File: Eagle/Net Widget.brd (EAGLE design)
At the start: 76.2 x 45.7 mm, 19 parts, among them IC1 ATmega1284P

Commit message: Tweak.
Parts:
- moved R1 26.5 mm to (71.8, 34.3)
- moved R2 6.55 mm to (47.3, 32.7)
- moved R3 6.55 mm to (47.3, 30.2)
- moved R5 6.55 mm to (47.3, 27.6)
- moved R6 0.64 mm to (67.6, 24.1)
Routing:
- net TOUCH: track 10.0 -> 9.40 mm
- net N$1: track 4.18 -> 3.55 mm
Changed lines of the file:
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@@
 <vertex x="62.23" y="35.56"/>
 </polygon>
-<rectangle x1="69.85" y1="17.78" x2="76.2" y2="29.21" layer="41"/>
 <polygon width="0.4064" layer="42">
 <vertex x="76.2" y="29.21"/>
-<vertex x="69.85" y="29.21"/>
-<vertex x="69.85" y="25.0825"/>
+<vertex x="68.58" y="29.21"/>
+<vertex x="68.58" y="25.0825"/>
 <vertex x="62.23" y="25.0825"/>
 <vertex x="62.23" y="23.495"/>
 <vertex x="64.4525" y="23.495"/>
 <vertex x="64.4525" y="21.9075"/>
-<vertex x="69.85" y="21.9075"/>
-<vertex x="69.85" y="17.78"/>
+<vertex x="68.58" y="21.9075"/>
+<vertex x="68.58" y="17.78"/>
 <vertex x="76.2" y="17.78"/>
+</polygon>
+<polygon width="0.4064" layer="41">
+<vertex x="76.2" y="17.78"/>
+<vertex x="68.58" y="17.78"/>
+<vertex x="68.58" y="29.21"/>
+<vertex x="76.2" y="29.21"/>
 </polygon>
 </plain>
@@
 <element name="LED1" library="SparkFun-LED" package="LED-TRICOLOR-5050" value="LED-TRICOLOR-5050NO_IC" x="38.1" y="22.86" rot="R180"/>
 <element name="LED2" library="led" package="1206" value="" x="71.755" y="31.4325"/>
-<element name="R1" library="rcl" package="R1206" value="100" x="45.72" y="29.21"/>
-<element name="R2" library="rcl" package="R1206" value="100" x="45.72" y="26.3525"/>
-<element name="R3" library="rcl" package="R1206" value="100" x="45.72" y="23.8125"/>
-<element name="R5" library="rcl" package="R1206" value="100" x="45.72" y="21.2725"/>
-<element name="R6" library="rcl" package="R1206" value="1M" x="68.2625" y="24.13" rot="R180"/>
+<element name="R1" library="rcl" package="R1206" value="100" x="71.755" y="34.29"/>
+<element name="R2" library="rcl" package="R1206" value="100" x="47.3075" y="32.7025"/>
+<element name="R3" library="rcl" package="R1206" value="100" x="47.3075" y="30.1625"/>
+<element name="R5" library="rcl" package="R1206" value="100" x="47.3075" y="27.6225"/>
+<element name="R6" library="rcl" package="R1206" value="1M" x="67.6275" y="24.13" rot="R180"/>
 </elements>
 <signals>
@@
 <contactref element="IC1" pad="13"/>
 <contactref element="R1" pad="2"/>
-<wire x1="47.142" y1="29.21" x2="51.6675" y2="31.14" width="0" layer="19" extent="1-1"/>
+<wire x1="73.177" y1="34.29" x2="51.6675" y2="31.14" width="0" layer="19" extent="1-1"/>
 </signal>
 <signal name="B">
 <contactref element="IC1" pad="14"/>
 <contactref element="R2" pad="2"/>
-<wire x1="47.142" y1="26.3525" x2="51.6675" y2="30.34" width="0" layer="19" extent="1-1"/>
+<wire x1="48.7295" y1="32.7025" x2="51.6675" y2="30.34" width="0" layer="19" extent="1-1"/>
 </signal>
 <signal name="R">
 <contactref element="IC1" pad="15"/>
 <contactref element="R3" pad="2"/>
-<wire x1="47.142" y1="23.8125" x2="51.6675" y2="29.54" width="0" layer="19" extent="1-1"/>
+<wire x1="48.7295" y1="30.1625" x2="51.6675" y2="29.54" width="0" layer="19" extent="1-1"/>
 </signal>
 <signal name="G">
 <contactref element="IC1" pad="16"/>
 <contactref element="R5" pad="2"/>
-<wire x1="47.142" y1="21.2725" x2="51.6675" y2="28.74" width="0" layer="19" extent="1-1"/>
+<wire x1="48.7295" y1="27.6225" x2="51.6675" y2="28.74" width="0" layer="19" extent="1-1"/>
 </signal>
 <signal name="N$9">
 <contactref element="R1" pad="1"/>
 <contactref element="LED2" pad="A"/>
-<wire x1="44.298" y1="29.21" x2="70.333" y2="31.4325" width="0" layer="19" extent="1-1"/>
+<wire x1="70.333" y1="34.29" x2="70.333" y2="31.4325" width="0" layer="19" extent="1-1"/>
 </signal>
 <signal name="TOUCH">
@@
 <polygon width="0.4064" layer="1">
 <vertex x="76.2" y="29.21"/>
-<vertex x="69.85" y="29.21"/>
-<vertex x="69.85" y="17.78"/>
+<vertex x="68.8975" y="29.21"/>
+<vertex x="68.8975" y="17.78"/>
 <vertex x="76.2" y="17.78"/>
 </polygon>
@@
 <wire x1="63.2675" y1="23.94" x2="64.77" y2="23.94" width="0.3048" layer="1"/>
 <wire x1="64.77" y1="23.94" x2="64.77" y2="22.225" width="0.3048" layer="1"/>
-<wire x1="64.77" y1="22.225" x2="69.6845" y2="22.225" width="0.3048" layer="1"/>
-<wire x1="69.6845" y1="22.225" x2="69.6845" y2="24.13" width="0.3048" layer="1"/>
+<wire x1="64.77" y1="22.225" x2="69.0495" y2="22.225" width="0.3048" layer="1"/>
+<wire x1="69.0495" y1="22.225" x2="69.0495" y2="24.13" width="0.3048" layer="1"/>
 </signal>
 <signal name="N$1">
 <contactref element="IC1" pad="35"/>
 <contactref element="R6" pad="2"/>
-<wire x1="63.2675" y1="24.74" x2="66.8405" y2="24.74" width="0.3048" layer="1"/>
-<wire x1="66.8405" y1="24.74" x2="66.8405" y2="24.13" width="0.3048" layer="1"/>
+<wire x1="63.2675" y1="24.74" x2="66.2055" y2="24.74" width="0.3048" layer="1"/>
+<wire x1="66.2055" y1="24.74" x2="66.2055" y2="24.13" width="0.3048" layer="1"/>
 </signal>
 <signal name="N$2">
 <contactref element="R3" pad="1"/>
 <contactref element="LED1" pad="2"/>
-<wire x1="40.5" y1="22.86" x2="44.298" y2="23.8125" width="0" layer="19" extent="1-1"/>
+<wire x1="40.5" y1="22.86" x2="45.8855" y2="30.1625" width="0" layer="19" extent="1-1"/>
 </signal>
 <signal name="N$4">
 <contactref element="R5" pad="1"/>
 <contactref element="LED1" pad="1"/>
-<wire x1="40.5" y1="21.16" x2="44.298" y2="21.2725" width="0" layer="19" extent="1-1"/>
+<wire x1="40.5" y1="21.16" x2="45.8855" y2="27.6225" width="0" layer="19" extent="1-1"/>
 </signal>
 <signal name="N$5">
 <contactref element="R2" pad="1"/>
 <contactref element="LED1" pad="3"/>
-<wire x1="40.5" y1="24.56" x2="44.298" y2="26.3525" width="0" layer="19" extent="1-1"/>
+<wire x1="40.5" y1="24.56" x2="45.8855" y2="32.7025" width="0" layer="19" extent="1-1"/>
 </signal>
 </signals>

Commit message: ...
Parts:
- moved R1 24.5 mm to (47.3, 33.0)
- moved R4 6.74 mm to (60.0, 34.0), turned to 180 degrees
- moved C1 5.39 mm to (48.3, 13.0)
- moved IC1 2.54 mm to (57.5, 25.4)
- moved R3 2.54 mm to (47.3, 27.6)
- moved C5 2.54 mm to (58.1, 16.5)
- moved R2 2.54 mm to (47.3, 30.2)
- moved R5 2.54 mm to (47.3, 25.1)
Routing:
- net N$6: track 0.00 -> 7.03 mm
- net N$7: track 0.00 -> 6.83 mm
- net N$1: track 3.55 -> 5.53 mm
- net TOUCH: track 9.40 -> 8.51 mm

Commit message: Route.
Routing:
- net GND: track 10.2 -> 182.3 mm, vias 0 -> 1
- net VCC: track 0.00 -> 123.7 mm, vias 0 -> 4
- net CS: track 0.00 -> 92.8 mm
- net IRQ: track 0.00 -> 84.3 mm, vias 0 -> 2
- net MOSI: track 0.00 -> 78.5 mm, vias 0 -> 1
- net VBEN: track 0.00 -> 74.4 mm, vias 0 -> 2
- net RESET: track 0.00 -> 69.5 mm
- net SCK: track 0.00 -> 62.5 mm
- net MISO: track 0.00 -> 57.7 mm, vias 0 -> 1
- net TX: track 0.00 -> 34.3 mm, vias 0 -> 1
- net N$9: track 0.00 -> 28.6 mm, vias 0 -> 2
- net RX: track 0.00 -> 22.5 mm
- net N$5: track 0.00 -> 7.86 mm
- net N$2: track 0.00 -> 7.37 mm
- net N$4: track 0.00 -> 7.02 mm
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
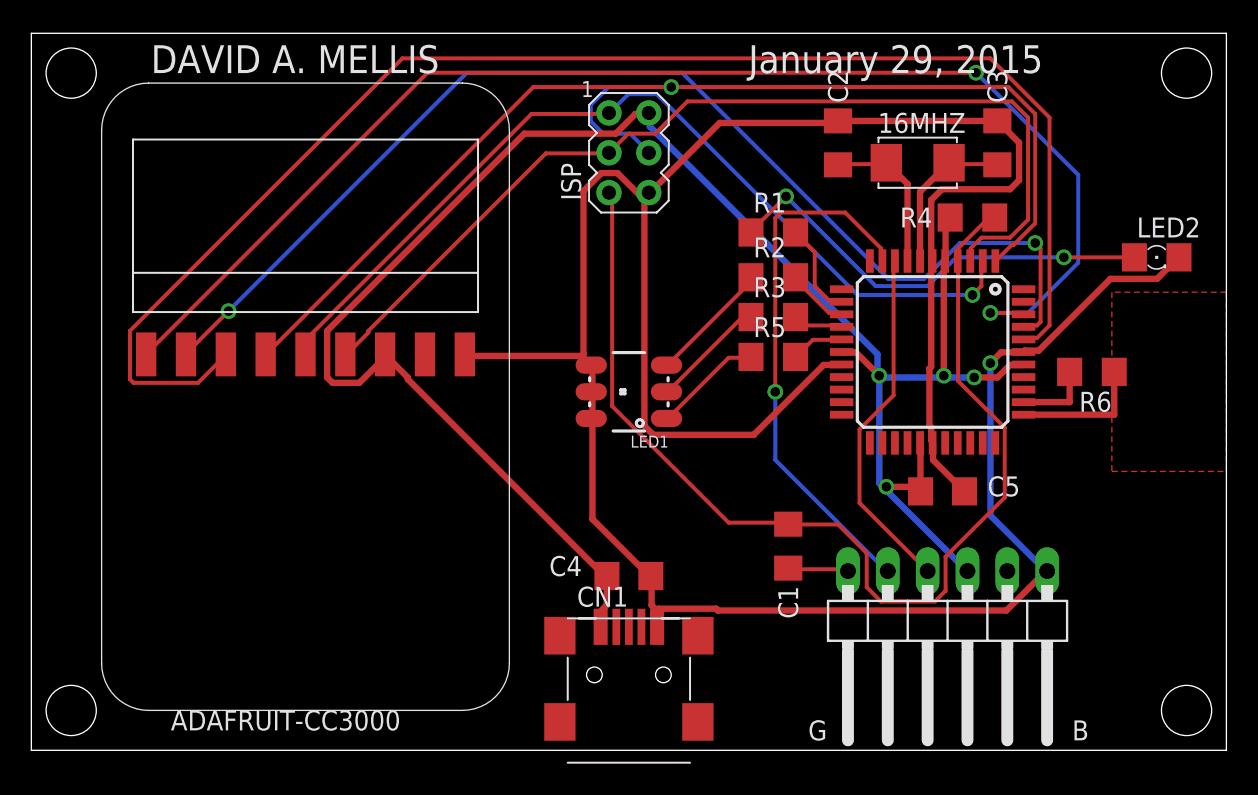
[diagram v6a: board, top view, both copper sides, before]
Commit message: Add alligator clip connector and adjust silkscreen
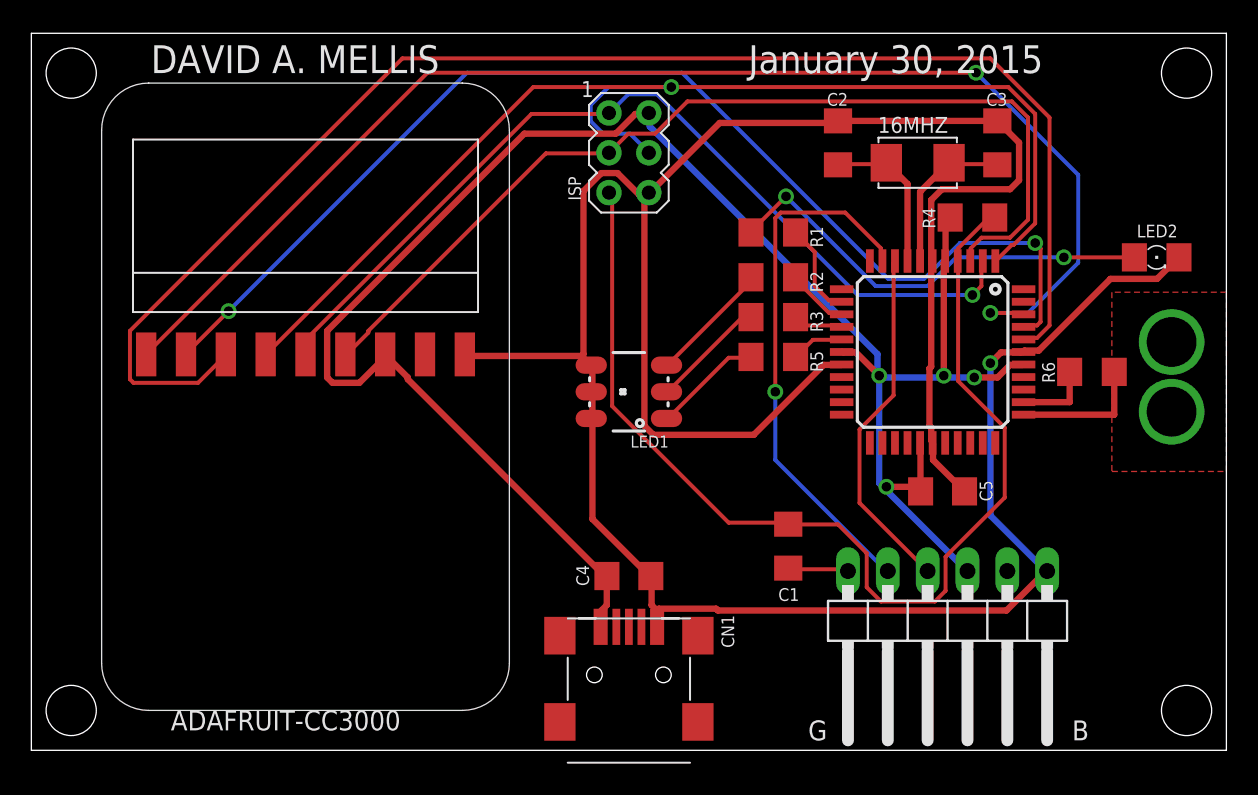
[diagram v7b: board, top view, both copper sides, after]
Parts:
- added TOUCH: (no value), SparkFun-Connectors:1X01_ALLIGATOR_3MM
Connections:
- net TOUCH: now also TOUCH.1@0, TOUCH.1@2
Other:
- board text added: "January 30, 2015"
- board text removed: "January 29, 2015"
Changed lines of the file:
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@@
 <layer number="27" name="tValues" color="7" fill="1" visible="yes" active="yes"/>
 <layer number="28" name="bValues" color="7" fill="1" visible="yes" active="yes"/>
-<layer number="29" name="tStop" color="7" fill="3" visible="no" active="yes"/>
-<layer number="30" name="bStop" color="7" fill="6" visible="no" active="yes"/>
+<layer number="29" name="tStop" color="7" fill="3" visible="yes" active="yes"/>
+<layer number="30" name="bStop" color="7" fill="6" visible="yes" active="yes"/>
 <layer number="31" name="tCream" color="7" fill="4" visible="no" active="yes"/>
 <layer number="32" name="bCream" color="7" fill="5" visible="no" active="yes"/>
@@
 <text x="8.89" y="1.27" size="1.27" layer="25" font="fixed">ADAFRUIT-CC3000</text>
 <text x="7.62" y="43.18" size="1.778" layer="25" font="fixed">DAVID A. MELLIS</text>
-<text x="45.72" y="43.18" size="1.778" layer="25" font="fixed">January 29, 2015</text>
+<text x="45.72" y="43.18" size="1.778" layer="25" font="fixed">January 30, 2015</text>
 <text x="66.3575" y="0.635" size="1.27" layer="25" font="fixed" rot="SR0">B</text>
 <text x="49.53" y="0.635" size="1.27" layer="25" font="fixed" rot="SR0">G</text>
@@
 <elements>
 <element name="C2" library="rcl" package="C1206" value="18pF" x="51.435" y="38.735" smashed="yes" rot="R270">
-<attribute name="NAME" x="52.07" y="41.275" size="1.27" layer="25" font="fixed" rot="R90"/>
-<attribute name="VALUE" x="49.2125" y="40.9575" size="1.27" layer="27" font="fixed" rot="R270"/>
+<attribute name="NAME" x="52.07" y="41.91" size="0.8128" layer="25" font="fixed" rot="R180"/>
+<attribute name="VALUE" x="49.2125" y="40.9575" size="1.016" layer="27" font="fixed" rot="R270"/>
 </element>
 <element name="C3" library="rcl" package="C1206" value="18pF" x="61.595" y="38.735" smashed="yes" rot="R270">
-<attribute name="NAME" x="62.23" y="41.275" size="1.27" layer="25" font="fixed" rot="R90"/>
-<attribute name="VALUE" x="62.5475" y="40.9575" size="1.27" layer="27" font="fixed" rot="R270"/>
+<attribute name="NAME" x="62.23" y="41.91" size="0.8128" layer="25" font="fixed" rot="R180"/>
+<attribute name="VALUE" x="62.5475" y="40.3225" size="1.016" layer="27" font="fixed" rot="R270"/>
 </element>
 <element name="ISP" library="adafruit" package="AVRISP" value="AVRISP-6" x="38.1" y="38.1" smashed="yes">
-<attribute name="NAME" x="35.052" y="35.052" size="1.27" layer="25" font="fixed" rot="R90"/>
+<attribute name="NAME" x="35.052" y="35.052" size="0.8128" layer="25" font="fixed" rot="R90"/>
 </element>
 <element name="U$2" library="Net Widget" package="ADAFRUIT-CC3000-BREAKOUT-RA" value="ADAFRUIT-CC3000-BREAKOUTRA" x="30.48" y="42.545" rot="R180"/>
 <element name="C4" library="rcl" package="C1206" value="10uF" x="38.1" y="11.1125" smashed="yes">
-<attribute name="NAME" x="33.02" y="11.1125" size="1.27" layer="25" font="fixed"/>
-<attribute name="VALUE" x="35.56" y="12.3825" size="1.27" layer="27" font="fixed"/>
+<attribute name="NAME" x="35.56" y="10.4775" size="0.8128" layer="25" font="fixed" rot="R90"/>
+<attribute name="VALUE" x="35.56" y="12.3825" size="1.016" layer="27" font="fixed"/>
 </element>
 <element name="C5" library="rcl" package="C1206" value="0.1uF" x="58.1025" y="16.51" smashed="yes">
-<attribute name="NAME" x="60.96" y="16.1925" size="1.27" layer="25" font="fixed"/>
-<attribute name="VALUE" x="55.5625" y="14.2875" size="1.27" layer="27" font="fixed"/>
+<attribute name="NAME" x="61.2775" y="15.875" size="0.8128" layer="25" font="fixed" rot="R90"/>
+<attribute name="VALUE" x="56.1975" y="14.2875" size="1.016" layer="27" font="fixed"/>
 </element>
 <element name="16MHZ" library="Net Widget" package="2-SMD-5X3MM" value="CRYSTAL" x="56.515" y="37.465" smashed="yes">
-<attribute name="NAME" x="53.975" y="39.37" size="1.27" layer="25" font="fixed"/>
+<attribute name="NAME" x="53.975" y="39.37" size="1.016" layer="25" font="fixed"/>
 </element>
 <element name="R4" library="rcl" package="R1206" value="10K" x="60.0075" y="33.9725" smashed="yes" rot="R180">
-<attribute name="NAME" x="57.4675" y="34.6075" size="1.27" layer="25" rot="R180"/>
-<attribute name="VALUE" x="61.2775" y="36.195" size="1.27" layer="27" rot="R180"/>
+<attribute name="NAME" x="56.8325" y="34.6075" size="0.8128" layer="25" rot="R270"/>
+<attribute name="VALUE" x="63.1825" y="33.02" size="0.8128" layer="27" rot="R90"/>
 </element>
 <element name="IC1" library="avr-5" package="TQFP44" value="ATmega1284P" x="57.4675" y="25.4" smashed="yes" rot="R270">
-<attribute name="VALUE" x="47.9425" y="16.3274" size="1.778" layer="27"/>
+<attribute name="VALUE" x="53.975" y="21.0899" size="0.8128" layer="27"/>
 </element>
 <element name="JP5" library="Net Widget" package="1X06/90" value="FTDI" x="58.42" y="7.62" smashed="yes" rot="R180">
@@
 </element>
 <element name="C1" library="rcl" package="C1206" value="0.1uF" x="48.26" y="13.0175" smashed="yes" rot="R270">
-<attribute name="NAME" x="47.625" y="10.4775" size="1.27" layer="25" rot="R270"/>
-<attribute name="VALUE" x="45.72" y="15.5575" size="1.27" layer="27" rot="R270"/>
-</element>
-<element name="CN1" library="Net Widget" package="USB-MINIB-POWER" value="" x="38.1" y="2.54"/>
-<element name="LED1" library="SparkFun-LED" package="LED-TRICOLOR-5050" value="LED-TRICOLOR-5050NO_IC" x="38.1" y="22.86" rot="R180"/>
-<element name="LED2" library="led" package="1206" value="" x="71.755" y="31.4325"/>
-<element name="R1" library="rcl" package="R1206" value="100" x="47.3075" y="33.02"/>
-<element name="R2" library="rcl" package="R1206" value="100" x="47.3075" y="30.1625"/>
-<element name="R3" library="rcl" package="R1206" value="100" x="47.3075" y="27.6225"/>
-<element name="R5" library="rcl" package="R1206" value="100" x="47.3075" y="25.0825"/>
-<element name="R6" library="rcl" package="R1206" value="1M" x="67.6275" y="24.13" rot="R180"/>
+<attribute name="NAME" x="47.625" y="9.525" size="0.8128" layer="25"/>
+<attribute name="VALUE" x="46.0375" y="14.9225" size="1.016" layer="27" rot="R270"/>
+</element>
+<element name="CN1" library="Net Widget" package="USB-MINIB-POWER" value="" x="38.1" y="2.54" smashed="yes">
+<attribute name="NAME" x="44.815" y="6.5325" size="0.8128" layer="25" rot="R90"/>
+<attribute name="VALUE" x="34.79" y="-2.54" size="1.27" layer="27"/>
+</element>
+<element name="LED1" library="SparkFun-LED" package="LED-TRICOLOR-5050" value="LED-TRICOLOR-5050NO_IC" x="38.1" y="22.86" smashed="yes" rot="R180">
+<attribute name="NAME" x="40.64" y="20.066" size="0.762" layer="25" rot="R180"/>
+<attribute name="VALUE" x="33.274" y="29.21" size="0.762" layer="27" rot="R270"/>
+</element>
+<element name="LED2" library="led" package="1206" value="" x="71.755" y="31.4325" smashed="yes">
+<attribute name="NAME" x="70.485" y="32.7025" size="0.8128" layer="25"/>
+<attribute name="VALUE" x="70.485" y="28.8925" size="1.27" layer="27"/>
+</element>
+<element name="R1" library="rcl" package="R1206" value="100" x="47.3075" y="33.02" smashed="yes">
+<attribute name="NAME" x="50.4825" y="32.0675" size="0.8128" layer="25" rot="R90"/>
+<attribute name="VALUE" x="44.7675" y="31.75" size="1.016" layer="27" rot="R90"/>
+</element>
+<element name="R2" library="rcl" package="R1206" value="100" x="47.3075" y="30.1625" smashed="yes">
+<attribute name="NAME" x="50.4825" y="29.21" size="0.8128" layer="25" rot="R90"/>
+<attribute name="VALUE" x="44.7675" y="28.8925" size="1.016" layer="27" rot="R90"/>
+</element>
+<element name="R3" library="rcl" package="R1206" value="100" x="47.3075" y="27.6225" smashed="yes">
+<attribute name="NAME" x="50.4825" y="26.67" size="0.8128" layer="25" rot="R90"/>
+<attribute name="VALUE" x="44.7675" y="26.3525" size="1.016" layer="27" rot="R90"/>
+</element>
+<element name="R5" library="rcl" package="R1206" value="100" x="47.3075" y="25.0825" smashed="yes">
+<attribute name="NAME" x="50.4825" y="24.13" size="0.8128" layer="25" rot="R90"/>
+<attribute name="VALUE" x="44.7675" y="23.8125" size="1.016" layer="27" rot="R90"/>
+</element>
+<element name="R6" library="rcl" package="R1206" value="1M" x="67.6275" y="24.13" smashed="yes" rot="R180">
+<attribute name="NAME" x="64.4525" y="24.765" size="0.8128" layer="25" rot="R270"/>
+<attribute name="VALUE" x="68.58" y="26.3525" size="1.016" layer="27" rot="R180"/>
+</element>
+<element name="TOUCH" library="SparkFun-Connectors" package="1X01_ALLIGATOR_3MM" value="" x="72.7075" y="23.8125"/>
 </elements>
 <signals>
@@
 <wire x1="63.2675" y1="21.4" x2="69.0495" y2="21.4" width="0.4064" layer="1"/>
 <wire x1="69.0495" y1="21.4" x2="69.0495" y2="24.13" width="0.4064" layer="1"/>
+<contactref element="TOUCH" pad="1@2"/>
+<contactref element="TOUCH" pad="1@0"/>
 </signal>
 <signal name="N$1">
